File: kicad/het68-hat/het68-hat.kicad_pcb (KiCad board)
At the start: 4 copper layers, 99 x 96 mm, 91 parts, among them J1 MIC1, J10 PWR, J11 PZ1, J12 PZ2, J13 PZ3, J14 PZ4, J17 UART, J2 MIC2, J3 MIC3, J4 MIC4, J5 MIC5, J6 MIC6, U1 Pico_Plus_2, U2 SN74LVC8T245, U3 SN74LVC8T245, U4 SN74LVC8T245, U5 AP2112K-1.8, U6 DRV8837, U7 DPS310, U8 SHT40, U9 INA3221

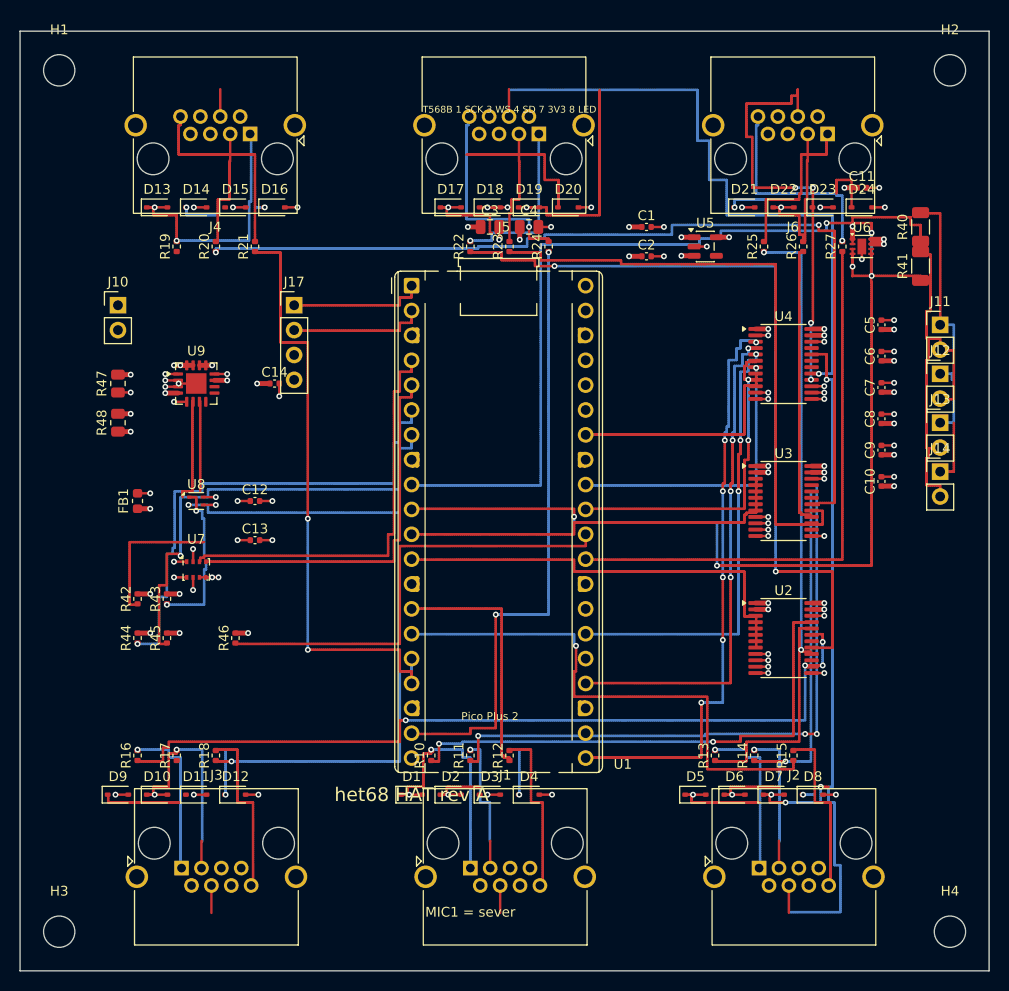
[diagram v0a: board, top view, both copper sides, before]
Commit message: Switch the boards to two layers and specify the power sources.
The HAT is no longer four-layer and the gerbers match that stackup. The power board now names the clamp CT, solar MPPT, 21700 cell and 5 V output; those charger parts are not drawn in KiCad yet.

Co-authored-by: Cursor <cursoragent@cursor.com>
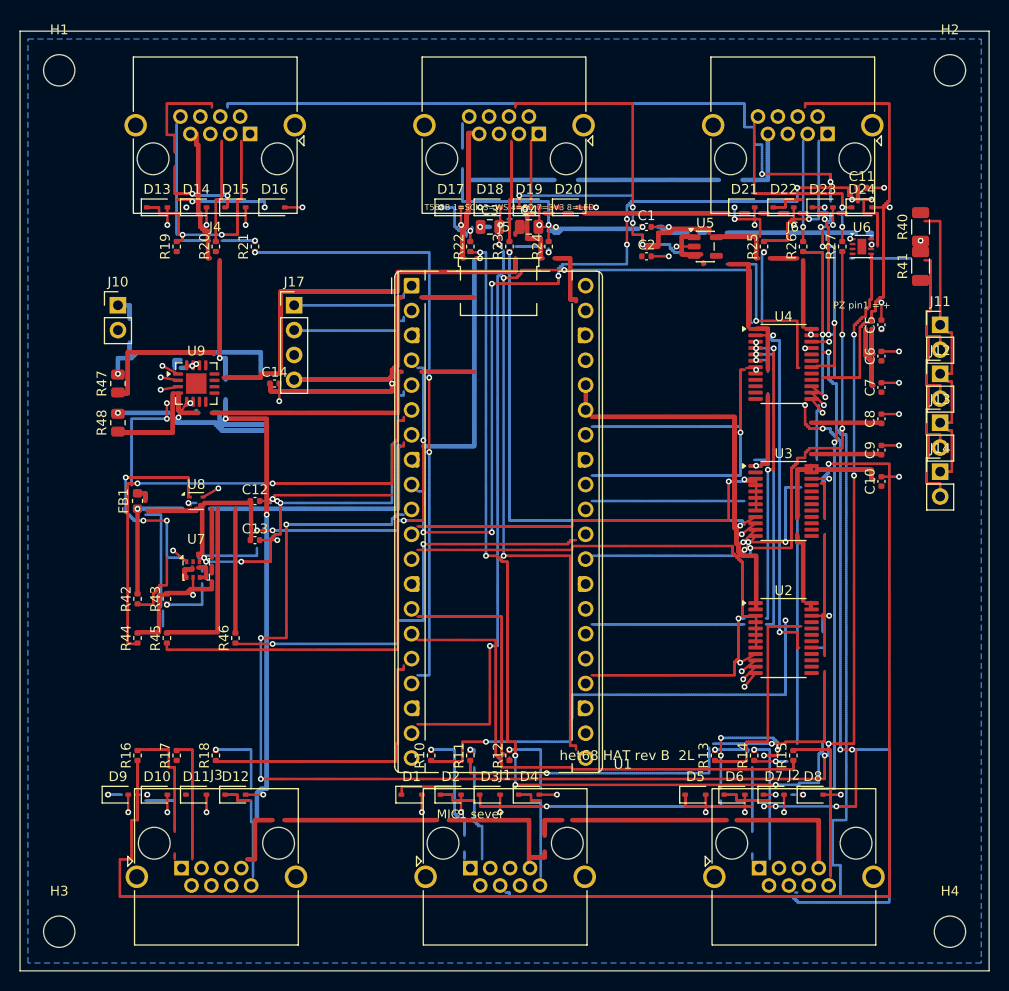
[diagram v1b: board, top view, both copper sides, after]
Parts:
- U6: value DRV8837 -> DRV8837C
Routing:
- net +3V3: track 32.5 -> 293.4 mm, vias 25 -> 8
- net +3V3_MIC: track 2.60 -> 217.4 mm, vias 2 -> 7
- net SD1_18: track 2.80 -> 156.0 mm, vias 0 -> 13
- net GND: track 88.9 -> 233.0 mm, vias 68 -> 65
- net SD4_18: track 2.80 -> 113.2 mm, vias 0 -> 7
- net WS4_B: track 97.1 -> 0.00 mm, vias 2 -> 0
- net VSYS: track 6.50 -> 99.0 mm, vias 5 -> 2
- net SCK3_B: track 84.3 -> 161.2 mm, vias 4 -> 1
- net PIEZO_IN2: track 84.7 -> 157.6 mm, vias 2 -> 7
- net SD5_18: track 88.9 -> 31.2 mm, vias 1 -> 2
- net +1V8: track 14.3 -> 52.4 mm, vias 11 -> 1
- net SD2_18: track 77.9 -> 107.2 mm
- net SD1_3V3: track 60.3 -> 87.4 mm, vias 6 -> 4
- net SD6_18: track 44.9 -> 20.2 mm, vias 4 -> 3
- net SCK5_B: track 79.7 -> 103.6 mm, vias 2 -> 5
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- added copper zone on B.Cu, net GND
- removed copper zone on In2.Cu, net +3V3
- removed copper zone on In1.Cu, net GND
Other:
- copper layers 4 -> 2
- board text added: "MIC1 sever"
- board text added: "PZ pin1 = +"
- board text added: "T568B 1=SCK 3=WS 4=SD 7=3V3 8=LED"
- board text added: "het68 HAT rev B 2L"
- board text removed: "MIC1 = sever"
- board text removed: "Pico Plus 2"
- board text removed: "T568B 1 SCK 3 WS 4 SD 7 3V3 8 LED"
- board text removed: "het68 HAT rev A"

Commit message: Reroute the two-layer boards and show the whole assembly.
The satellite now passes DRC, the power board no longer shorts, and the HAT parts sit beside the Pico instead of on it. Previews include the clamp on one mains conductor, the panel, the 21700 cell and the linked boards.

Co-authored-by: Cursor <cursoragent@cursor.com>
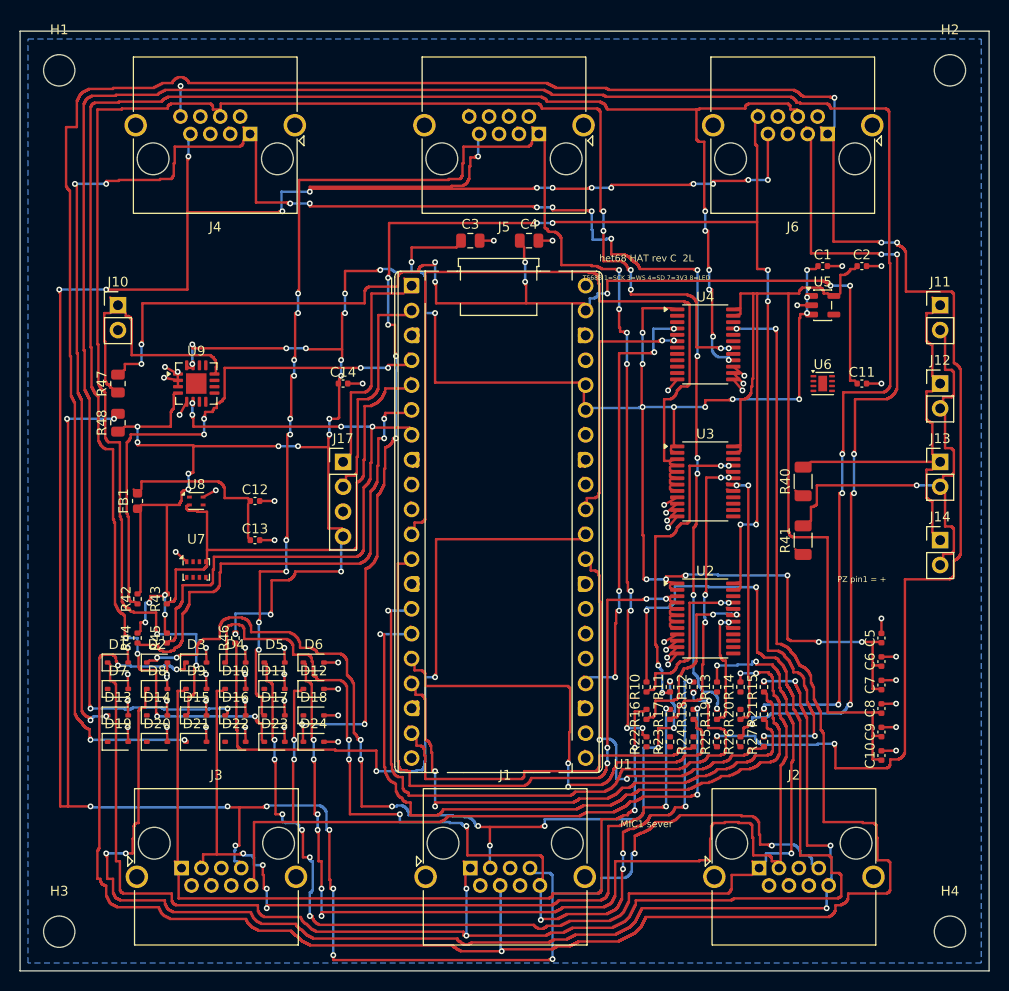
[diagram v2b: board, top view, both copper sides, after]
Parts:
- moved D21 78.2 mm to (18.0, 72.6)
- moved D22 78.2 mm to (22.0, 72.6)
- moved D23 78.2 mm to (26.0, 72.6)
- moved D24 78.2 mm to (30.0, 72.6)
- moved R19 73.0 mm to (71.2, 69.8)
- moved R20 71.8 mm to (73.6, 69.8)
- moved R21 70.6 mm to (76.0, 69.8)
- moved D19 68.9 mm to (10.0, 72.6)
- moved D20 68.9 mm to (14.0, 72.6)
- moved D7 67.9 mm to (10.0, 67.2)
- moved D8 67.9 mm to (14.0, 67.2)
- moved D17 54.9 mm to (26.0, 69.9)
- moved D18 54.9 mm to (30.0, 69.9)
- moved R22 53.7 mm to (64.0, 72.6)
- moved R23 53.2 mm to (66.4, 72.6)
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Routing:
- net SCK6: track 21.4 -> 270.2 mm, vias 3 -> 7
- net LED4: track 27.4 -> 241.4 mm, vias 3 -> 7
- net SD6_18: track 20.2 -> 188.5 mm, vias 3 -> 10
- net SCK4: track 23.2 -> 187.8 mm, vias 2 -> 16
- net PIEZO_IN2: track 157.6 -> 0.77 mm, vias 7 -> 0
- net SCK1: track 19.2 -> 175.4 mm, vias 1 -> 4
- net LED6: track 22.0 -> 176.3 mm, vias 2 -> 12
- net GND: track 233.0 -> 85.2 mm, vias 65 -> 57
- net SCK5: track 15.8 -> 160.5 mm, vias 3 -> 18
- net SCK3_B: track 161.2 -> 20.6 mm, vias 1 -> 2
- net +3V3_MIC: track 217.4 -> 343.3 mm, vias 7 -> 26
- net LED2: track 16.8 -> 137.1 mm, vias 1 -> 6
- net SD2_18: track 107.2 -> 0.72 mm, vias 3 -> 0
- net SCK5_B: track 103.6 -> 0.68 mm, vias 5 -> 0
- net SCK2: track 18.8 -> 117.1 mm, vias 1 -> 9
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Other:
- board text added: "het68 HAT rev C 2L"
- board text removed: "het68 HAT rev B 2L"

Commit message: Clear the remaining copper violations and add the order BOM.
HAT no longer reports shorts or clearance errors, and the power-board CC pins are connected. The order list now carries verified LCSC codes plus the power sources that are not drawn on the sheet yet.

Co-authored-by: Cursor <cursoragent@cursor.com>
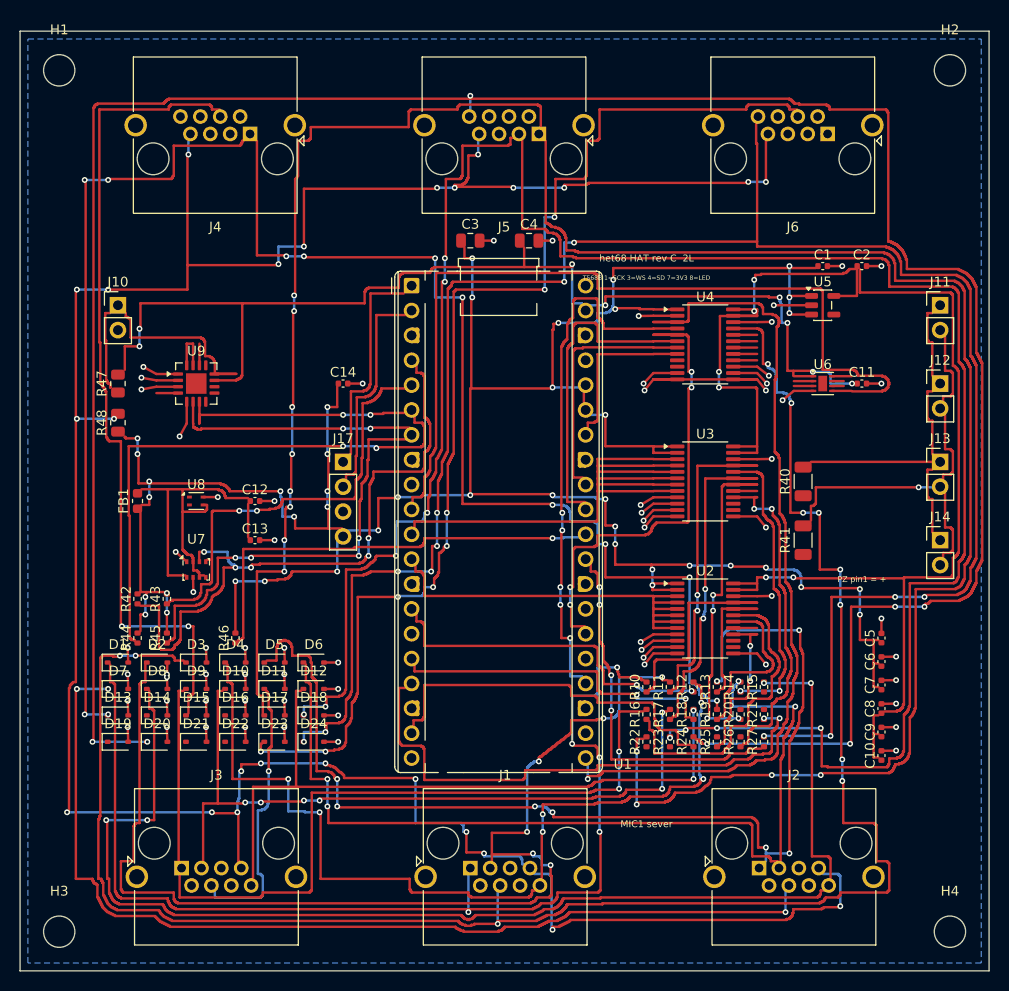
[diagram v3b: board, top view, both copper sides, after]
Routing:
- net SCK6: track 270.2 -> 0.59 mm, vias 7 -> 0
- net LED5: track 0.72 -> 260.3 mm, vias 0 -> 7
- net LED4: track 241.4 -> 0.59 mm, vias 7 -> 0
- net WS5: track 0.72 -> 225.5 mm, vias 0 -> 10
- net SD2_18: track 0.72 -> 107.8 mm, vias 0 -> 3
- net SD1_3V3: track 0.76 -> 92.1 mm, vias 0 -> 1
- net PIEZO_IN2: track 0.77 -> 90.6 mm
- net SCK5: track 160.5 -> 247.7 mm, vias 18 -> 12
- net WS6: track 86.4 -> 0.60 mm, vias 6 -> 0
- net GND: track 85.2 -> 168.7 mm, vias 57 -> 66
- net SD4_18: track 165.3 -> 88.3 mm, vias 8 -> 2
- net LED2_G: track 76.6 -> 0.64 mm, vias 1 -> 0
- net SD6_18: track 188.5 -> 125.5 mm, vias 10 -> 8
- net +3V3_MIC: track 343.3 -> 282.0 mm, vias 26 -> 25
- net SCK1: track 175.4 -> 116.3 mm, vias 4 -> 5
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
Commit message: Shrink the acoustic board and ground the cable shield only at the HAT.
The HAT outline is 94 by 96 mm and the satellite shell pin is open. The README drops the power-board LED note and estimates a self-built Pico Plus 2 W against the bought module.

Co-authored-by: Cursor <cursoragent@cursor.com>
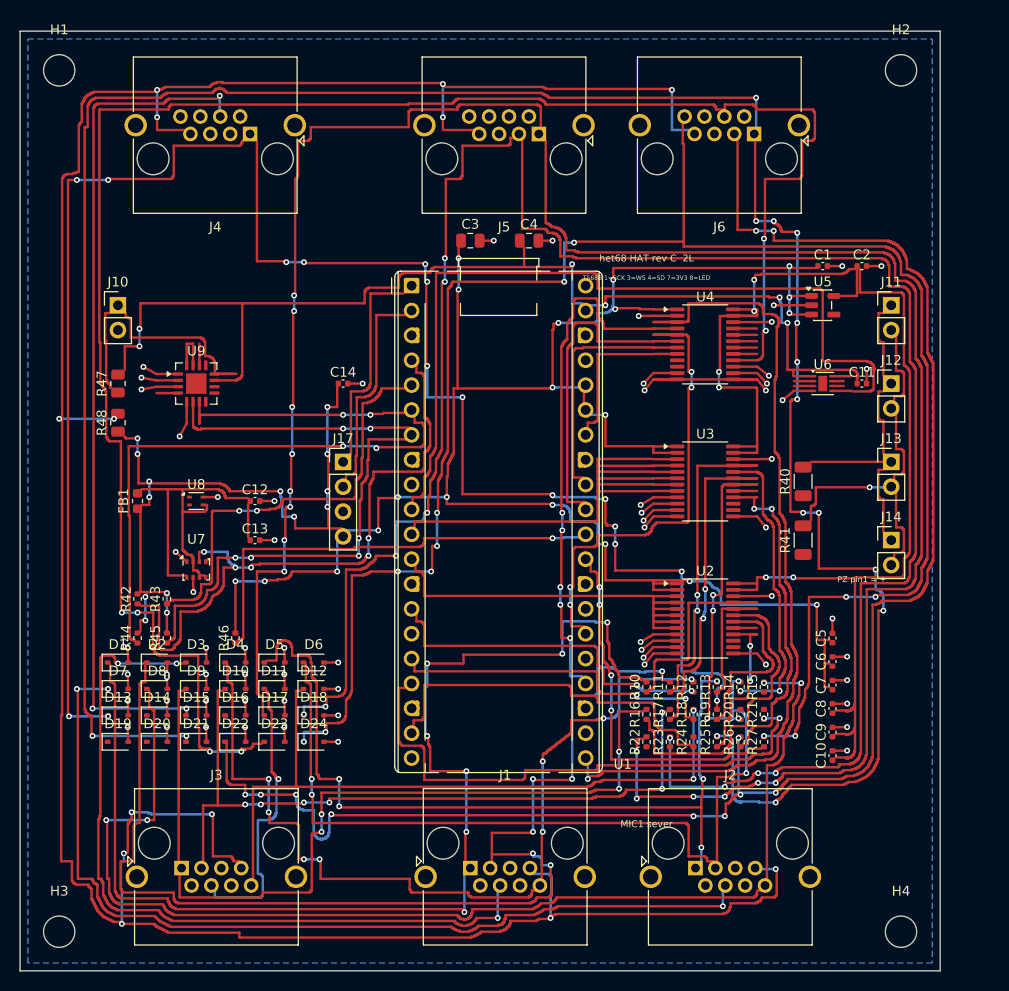
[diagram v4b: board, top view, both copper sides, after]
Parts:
- moved J6 7.50 mm to (75.0, 10.5)
- moved J2 6.50 mm to (69.0, 85.5)
- moved C10 5.00 mm to (83.0, 74.0)
- moved C5 5.00 mm to (83.0, 62.0)
- moved C6 5.00 mm to (83.0, 64.4)
- moved C7 5.00 mm to (83.0, 66.8)
- moved C8 5.00 mm to (83.0, 69.2)
- moved C9 5.00 mm to (83.0, 71.6)
- moved H2 5.00 mm to (90.0, 4.00)
- moved H4 5.00 mm to (90.0, 92.0)
- moved J11 5.00 mm to (89.0, 28.0)
- moved J12 5.00 mm to (89.0, 36.0)
- moved J13 5.00 mm to (89.0, 44.0)
- moved J14 5.00 mm to (89.0, 52.0)
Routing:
- net LED5: track 260.3 -> 0.59 mm, vias 7 -> 0
- net SCK6: track 0.59 -> 256.7 mm, vias 0 -> 15
- net WS6: track 0.60 -> 180.6 mm, vias 0 -> 11
- net SD1_18: track 199.0 -> 84.6 mm, vias 11 -> 3
- net SD6_18: track 125.5 -> 194.3 mm, vias 8 -> 6
- net SCK2: track 117.5 -> 85.2 mm, vias 8 -> 5
- net +3V3_MIC: track 282.0 -> 299.8 mm, vias 25 -> 13
- net SCK5: track 247.7 -> 236.5 mm, vias 12 -> 14
- net WS2: track 96.1 -> 86.1 mm
- net LED6: track 204.9 -> 194.9 mm
- net WS5: track 225.5 -> 217.5 mm
- net SCK1: track 116.3 -> 123.3 mm, vias 5 -> 7
- net SD2_18: track 107.8 -> 101.2 mm
- net LED2: track 132.8 -> 126.8 mm
- net +3V3: track 301.2 -> 295.4 mm, vias 42 -> 34
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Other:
- board size 99 x 96 mm -> 94 x 96 mm

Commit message: Protect the CT secondary and ship clean power and satellite fab files.
Add burden, LC filter and crowbar on the power board, close DRC on power and satellite, and refresh the board previews for v1.10.0.

Co-authored-by: Cursor <cursoragent@cursor.com>
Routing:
- net +3V3_MIC: track 299.8 -> 0.00 mm, vias 13 -> 0
- net +3V3: track 295.4 -> 20.3 mm, vias 34 -> 1
- net SCK6: track 256.7 -> 0.00 mm, vias 15 -> 0
- net SCK5: track 236.5 -> 0.00 mm, vias 14 -> 0
- net WS5: track 217.5 -> 0.00 mm, vias 10 -> 0
- net LED6: track 194.9 -> 0.00 mm, vias 12 -> 0
- net SD6_18: track 194.3 -> 0.00 mm, vias 6 -> 0
- net SCK4: track 188.3 -> 0.00 mm, vias 16 -> 0
- net WS6: track 180.6 -> 0.00 mm, vias 11 -> 0
- net GND: track 168.7 -> 0.00 mm, vias 66 -> 0
- net +1V8: track 137.5 -> 0.00 mm, vias 6 -> 0
- net LED2: track 126.8 -> 0.00 mm, vias 4 -> 0
- net SCK1: track 123.3 -> 0.00 mm, vias 7 -> 0
- net WS1: track 122.5 -> 0.00 mm, vias 6 -> 0
- net VSYS: track 115.7 -> 0.00 mm, vias 6 -> 0
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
